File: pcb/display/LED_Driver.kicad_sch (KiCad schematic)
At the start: 26 parts, among them J5 Term, J6 Term, Q1 60N03D, Q2 60N03D, U3 TPS22810DRV, U4 TCA9535RGER

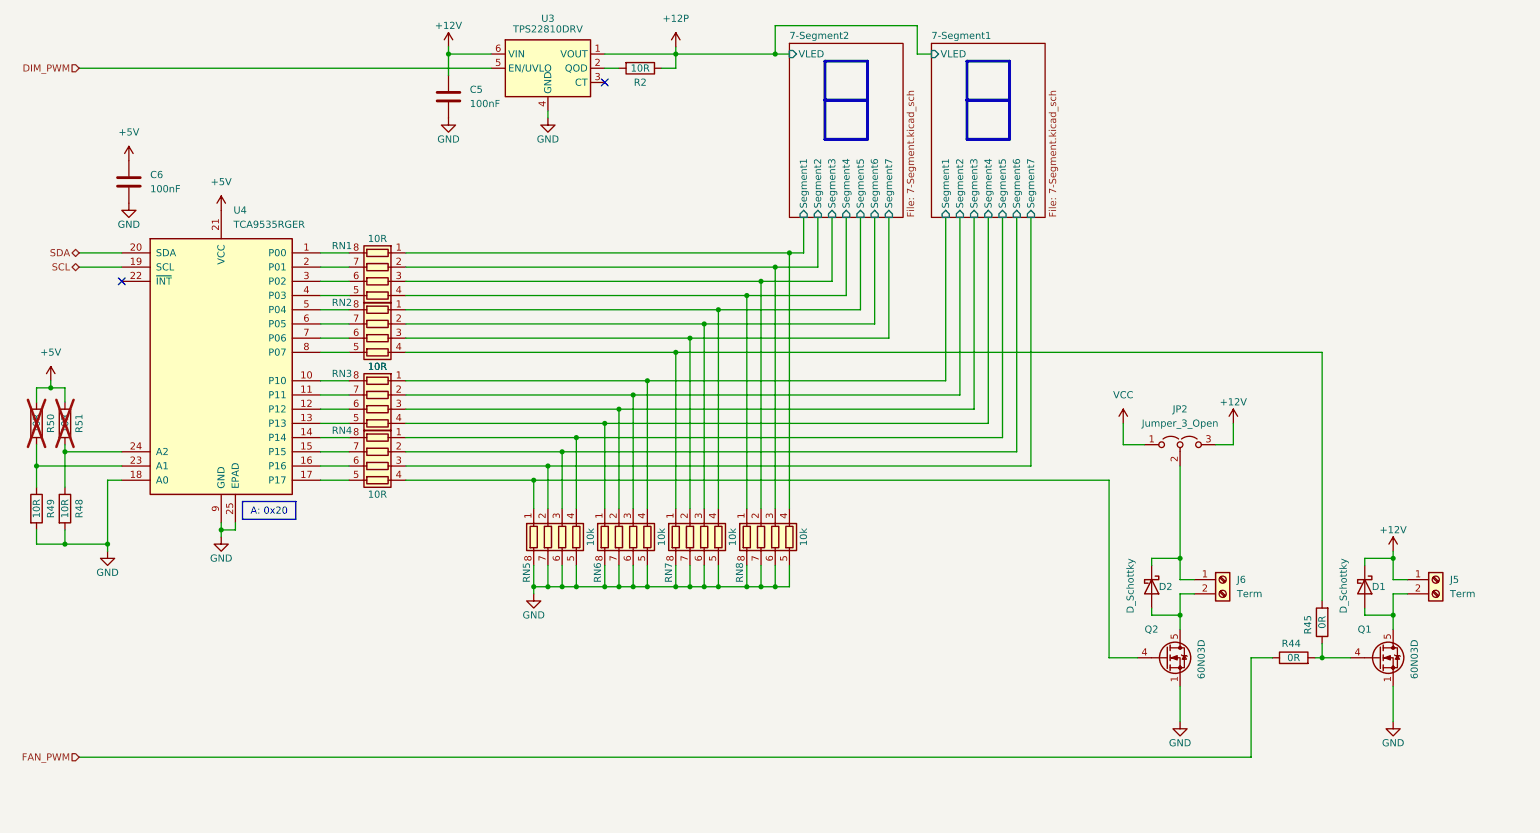
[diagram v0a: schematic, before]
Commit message: Final Version of Prototype Rev. 00
Switched back to PCA9685 for PWM, removed high side switch
Updated some component values
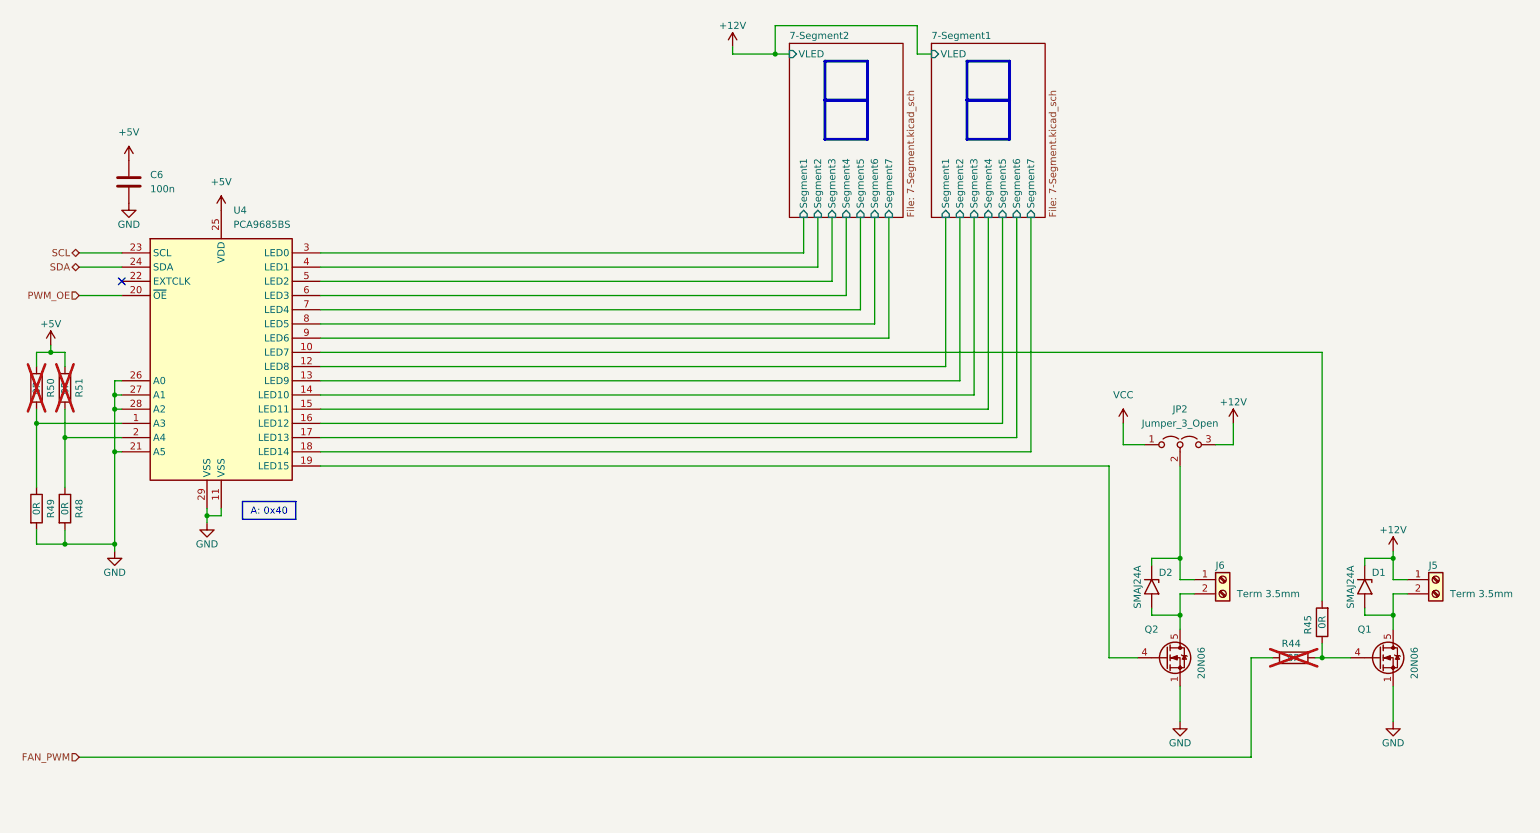
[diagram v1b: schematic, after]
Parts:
- removed C5: 100nF, Capacitor_SMD:C_0603_1608Metric, symbol Device:C
- removed D1, D2: D_Schottky, Diode_SMD:D_SMA, symbol Device:D_Schottky
- removed R2: 10R, Resistor_SMD:R_0603_1608Metric, symbol Device:R
- removed RN1, RN2, RN3, RN4: 10R, Resistor_SMD:R_Array_Convex_4x0603, symbol Device:R_Pack04
- removed RN5, RN6, RN7, RN8: 10k, Resistor_SMD:R_Array_Convex_4x0603, symbol Device:R_Pack04
- removed U3: TPS22810DRV, Package_SON:WSON-6-1EP_2x2mm_P0.65mm_EP1x1.6mm, symbol Power_Management:TPS22810DRV
- removed U4: TCA9535RGER, Package_DFN_QFN:VQFN-24-1EP_4x4mm_P0.5mm_EP2.45x2.45mm, symbol Interface_Expansion:TCA9535RGER
- added D1, D2: SMAJ24A, Diode_SMD:D_SMA, symbol Diode:SMAJ24A
- added U4: PCA9685BS, Package_DFN_QFN:QFN-28-1EP_6x6mm_P0.65mm_EP4.25x4.25mm, symbol Driver_LED:PCA9685BS
- C6: value 100nF -> 100n
- J5, J6: value Term -> Term 3.5mm
- Q1, Q2: value 60N03D -> 20N06
- R44: now not fitted
- R48, R49, R50, R51: value 10R -> 0R
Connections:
- net +12V: now also D1.1 (A1)
- net +5V: now also U4.25 (VDD)
- net 7-Segment1/Segment1: now also U4.12 (LED8)
- net 7-Segment1/Segment2: now also U4.13 (LED9)
- net 7-Segment1/Segment3: now also U4.14 (LED10)
- net 7-Segment1/Segment4: now also U4.15 (LED11)
- net 7-Segment1/Segment5: now also U4.16 (LED12)
- net 7-Segment1/Segment6: now also U4.17 (LED13)
- net 7-Segment1/Segment7: now also U4.18 (LED14)
- net 7-Segment2/Segment1: now also U4.3 (LED0)
- net 7-Segment2/Segment2: now also U4.4 (LED1)
- net 7-Segment2/Segment3: now also U4.5 (LED2)
- net 7-Segment2/Segment4: now also U4.6 (LED3)
- net 7-Segment2/Segment5: now also U4.7 (LED4)
- net 7-Segment2/Segment6: now also U4.8 (LED5)
- net 7-Segment2/Segment7: now also U4.9 (LED6)
- net GND: now also U4.11 (VSS), U4.21 (A5), U4.26 (A0), U4.27 (A1), U4.28 (A2), U4.29 (VSS)
- net SCL: now also U4.23 (SCL)
- net SDA: now also U4.24 (SDA)
- net at J6.1 (Pin_1), JP2.2 (C): now also D2.1 (A1)
- net at J6.2 (Pin_2), Q2.5 (D): now also D2.2 (A2)
- net at J5.2 (Pin_2), Q1.5 (D): now also D1.2 (A2)
- net at R48.1, R51.2: now also U4.2 (A4)
- net at R45.2: now also U4.10 (LED7)
- net at Q2.4 (G): now also U4.19 (LED15)
- net at R49.1, R50.2: now also U4.1 (A3)
- new net PWM_OE: U4.20 (~{OE})
- no-connect marks 2 -> 1
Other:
- moved on the sheet: R50, R51

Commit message: Marked known issues in schematic
Add gitignore
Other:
- note added: "Add LED to these Outputs"
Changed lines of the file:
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@@
+		)
+	)
+	(text "Add LED to these Outputs"
+		(exclude_from_sim no)
+		(at 238.76 152.4 0)
+		(effects
+			(font
+				(size 2 2)
+				(thickness 0.4)
+				(bold yes)
+				(color 255 153 0 1)
+			)
 		)
 	)

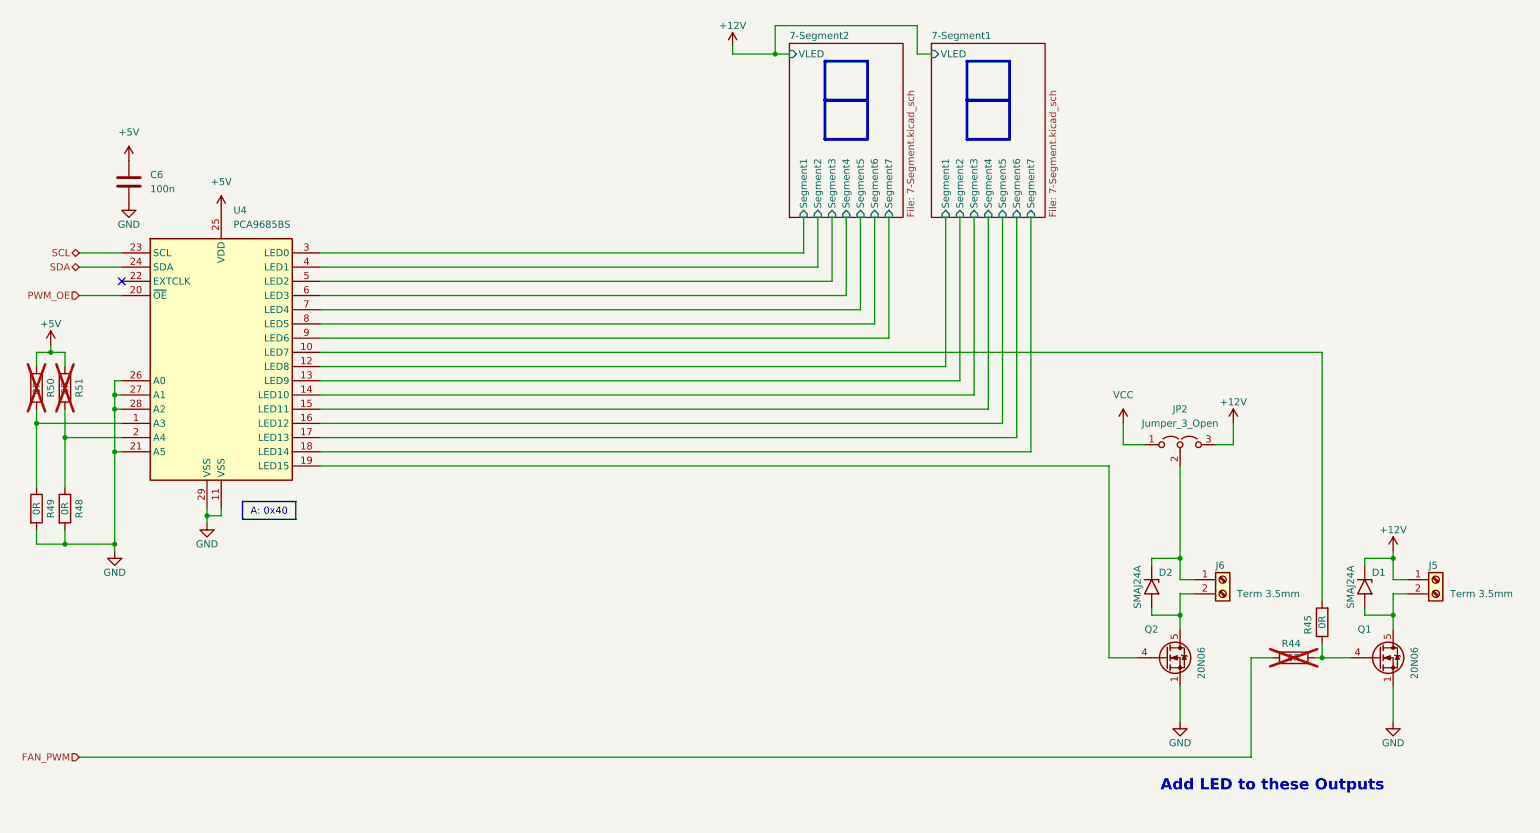
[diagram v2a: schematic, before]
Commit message: Display HW Revision 01
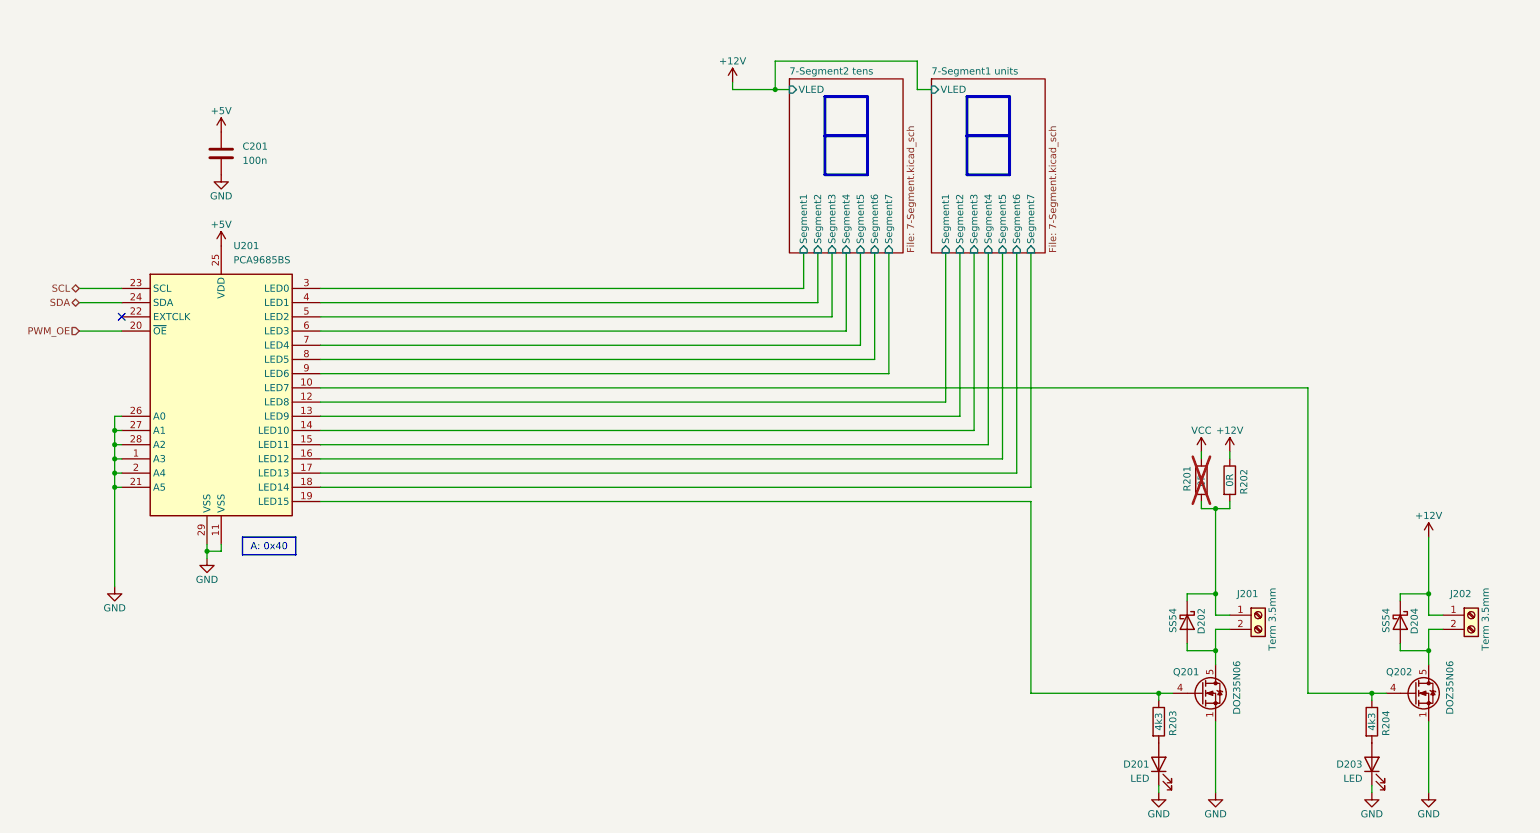
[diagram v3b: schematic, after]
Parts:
- removed D1: SMAJ24A, Diode_SMD:D_SMA, symbol Diode:SMAJ24A
- removed JP2: Jumper_3_Open, Connector_PinHeader_2.54mm:PinHeader_1x03_P2.54mm_Vertical, symbol Jumper:Jumper_3_Open
- removed R44, R45: 0R, Resistor_SMD:R_0603_1608Metric, symbol Device:R
- removed R48, R49, R50, R51: 0R, Resistor_SMD:R_0402_1005Metric, symbol Device:R
- added D201, D203: LED, LED_SMD:LED_0603_1608Metric, symbol Device:LED
- added D204: SS54, Diode_SMD:D_SMA, symbol Device:D_Schottky
- added R201, R202: 0R, Resistor_SMD:R_1206_3216Metric, symbol Device:R
- added R203, R204: 4k3, Resistor_SMD:R_0402_1005Metric, symbol Device:R
- C201: renamed from C6; footprint Capacitor_SMD:C_0603_1608Metric -> Capacitor_SMD:C_0402_1005Metric; JLC PN (none) -> C307331
- D202: renamed from D2; value SMAJ24A -> SS54; symbol Diode:SMAJ24A -> Device:D_Schottky; JLC PN (none) -> C22452
- J201: renamed from J6; JLC PN (none) -> C409115
- J202: renamed from J5; JLC PN (none) -> C409115
- Q201: renamed from Q2; value 20N06 -> DOZ35N06; JLC PN (none) -> C36499167
- Q202: renamed from Q1; value 20N06 -> DOZ35N06; JLC PN (none) -> C36499167
- U201: renamed from U4; JLC PN (none) -> C5191634
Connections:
- net +12V: now also D204.1 (K), R202.1
- net GND: now also U201.1 (A3), U201.2 (A4), D201.1 (K), D203.1 (K)
- net VCC: now also R201.2
- net at D202.1 (K), J201.1 (Pin_1): now also R201.1, R202.2
- net at Q202.4 (G): now also U201.10 (LED7), R204.1
- net at J202.2 (Pin_2), Q202.5 (D): now also D204.2 (A)
- net at Q201.4 (G), U201.19 (LED15): now also R203.1
- new net: D203.2 (A), R204.2
- new net: D201.2 (A), R203.2
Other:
- sheet 7-Segment1 renamed 7-Segment1 units
- sheet 7-Segment2 renamed 7-Segment2 tens
- note removed: "Add LED to these Outputs"
- moved on the sheet: C201, J201, J202, Q201, Q202, U201

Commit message: OSC Display Hardware Revision 02
There might still be some errors which need to be corrected during ordering.
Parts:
- C201: JLC PN C307331 -> (none); LCSC Part # (none) -> C307331
- D201, D203: JLC PN C2286 -> (none); LCSC Part # (none) -> C2286
- D202, D204: JLC PN C22452 -> (none); LCSC Part # (none) -> C22452
- J201, J202: JLC PN C409115 -> (none); LCSC Part # (none) -> C409115
- Q201, Q202: JLC PN C36499167 -> (none); LCSC Part # (none) -> C36499167
- U201: JLC PN C5191634 -> (none); LCSC Part # (none) -> C5191634
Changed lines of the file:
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@@
 	(title_block
 		(title "PWM LED Driver")
-		(date "2025-04-11")
-		(rev "01")
+		(date "2026-03-01")
+		(rev "02")
 		(company "Ravenspark")
 		(comment 1 "0-Series")
@@
 			)
 		)
-		(property "JLC PN" "C409115"
+		(property "LCSC Part #" "C409115"
 			(at 236.22 121.92 0)
 			(effects
@@
 			)
 		)
-		(property "JLC PN" "C36499167"
+		(property "LCSC Part #" "C36499167"
 			(at 264.16 135.89 0)
 			(effects
@@
 			)
 		)
-		(property "JLC PN" "C5191634"
+		(property "LCSC Part #" "C5191634"
 			(at 50.8 81.28 0)
 			(effects
@@
 			)
 		)
-		(property "JLC PN" "C22452"
+		(property "LCSC Part #" "C22452"
 			(at 261.62 123.19 0)
 			(effects
@@
 			)
 		)
-		(property "JLC PN" "C2286"
-			(at 256.54 148.59 0)
+		(property "LCSC Part #" "C2286"
+			(at 256.54 148.59 90)
 			(effects
 				(font
@@
 			)
 		)
-		(property "JLC PN" "C2286"
-			(at 218.44 148.59 0)
+		(property "LCSC Part #" "C2286"
+			(at 218.44 148.59 90)
 			(effects
 				(font
@@
 			)
 		)
-		(property "JLC PN" "C22452"
+		(property "LCSC Part #" "C22452"
 			(at 223.52 123.19 0)
 			(effects
@@
 			)
 		)
-		(property "JLC PN" "C307331"
+		(property "LCSC Part #" "C307331"
 			(at 50.8 39.37 0)
 			(effects
@@
 			)
 		)
-		(property "JLC PN" "C36499167"
+		(property "LCSC Part #" "C36499167"
 			(at 226.06 135.89 0)
 			(effects
@@
 			)
 		)
-		(property "JLC PN" "C409115"
+		(property "LCSC Part #" "C409115"
 			(at 274.32 121.92 0)
 			(effects

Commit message: Adjusted footprint of mosfets for 0.15mm solder mask spacing
New Gerber files
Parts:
- Q201, Q202: footprint Package_SON:VSON-8_3.3x3.3mm_P0.65mm_NexFET -> RVNSPRK_Packages:VSON-8_3.3x3.3mm_P0.65mm_Custom
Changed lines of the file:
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@@
 			)
 		)
-		(property "Footprint" "Package_SON:VSON-8_3.3x3.3mm_P0.65mm_NexFET"
+		(property "Footprint" "RVNSPRK_Packages:VSON-8_3.3x3.3mm_P0.65mm_Custom"
 			(at 269.24 133.35 0)
 			(effects
@@
 			)
 		)
-		(property "Footprint" "Package_SON:VSON-8_3.3x3.3mm_P0.65mm_NexFET"
+		(property "Footprint" "RVNSPRK_Packages:VSON-8_3.3x3.3mm_P0.65mm_Custom"
 			(at 231.14 133.35 0)
 			(effects
